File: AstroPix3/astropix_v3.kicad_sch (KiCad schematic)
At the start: 50 parts, among them J1 pcie_GECCO, J10 SPI_right, J2 ChipRings, J3 TempSens, J4 SFOut, J5 sample_clock_out, J6 HV_in_external, J7 Conn_01x03, J9 SPI_left, U2 SN65LVDS4, U5 AstroPix3_split

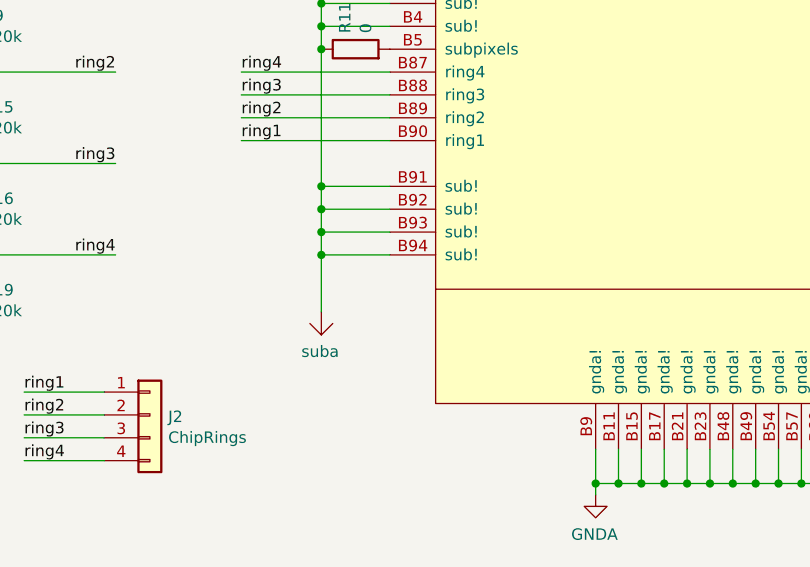
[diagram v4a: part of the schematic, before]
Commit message: PCB: Connected HV Pad
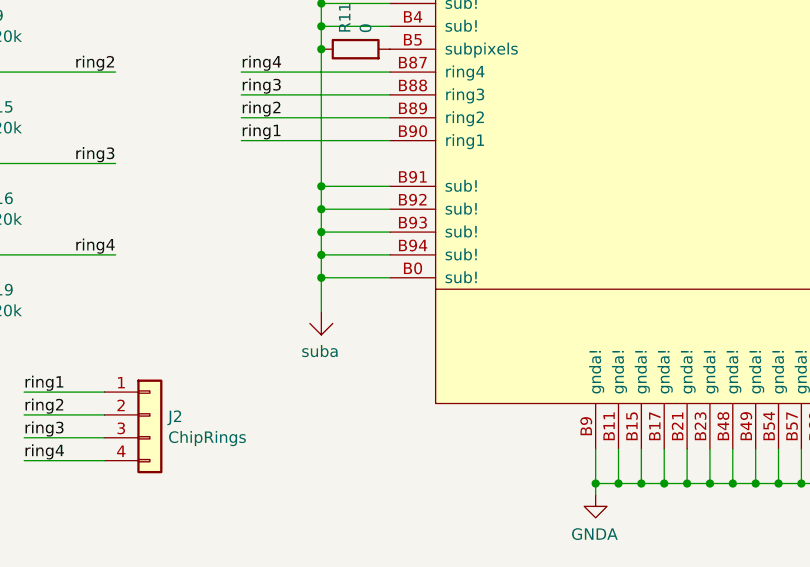
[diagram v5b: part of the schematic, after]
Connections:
- net suba: now also U5.B0 (sub!)
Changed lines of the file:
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@@
   (junction (at 309.88 236.22) (diameter 0) (color 0 0 0 0)
+  )
+  (junction (at 266.7 213.36) (diameter 0) (color 0 0 0 0)
   )
   (junction (at 266.7 203.2) (diameter 0) (color 0 0 0 0)
@@
     (stroke (width 0) (type default) (color 0 0 0 0))
   )
+  (wire (pts (xy 266.7 213.36) (xy 274.32 213.36))
+    (stroke (width 0) (type default) (color 0 0 0 0))
+  )
   (wire (pts (xy 266.7 208.28) (xy 266.7 205.74))
     (stroke (width 0) (type default) (color 0 0 0 0))
@@
     (stroke (width 0) (type default) (color 0 0 0 0))
   )
-  (wire (pts (xy 266.7 210.82) (xy 266.7 217.17))
+  (wire (pts (xy 266.7 210.82) (xy 266.7 213.36))
     (stroke (width 0) (type default) (color 0 0 0 0))
   )
@@
   )
   (wire (pts (xy 259.08 146.05) (xy 274.32 146.05))
+    (stroke (width 0) (type default) (color 0 0 0 0))
+  )
+  (wire (pts (xy 266.7 213.36) (xy 266.7 217.17))
     (stroke (width 0) (type default) (color 0 0 0 0))
   )
@@
     (pin "1")
   )
-  (symbol (lib_id "astropix:AstroPix3_split_power2") (at 304.8 144.78 0) (unit 1)
+  (symbol (lib_name "AstroPix3_split_power2_1") (lib_id "astropix:AstroPix3_split_power2") (at 304.8 144.78 0) (unit 1)
     (in_bom yes) (on_board yes) (fields_autoplaced)
     (property "Reference" "U5" (id 0) (at 370.84 126.7712 0))
@@
       (effects (font (size 1.27 1.27)) hide)
     )
+    (pin "B0")
     (pin "B1")
     (pin "B11")
@@
       (effects (font (size 1.27 1.27)) hide)
     )
+    (pin "B0")
     (pin "B1")
     (pin "B11")

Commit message: PCB: V3 improvements
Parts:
- removed R1: 0, Resistor_SMD:R_1206_3216Metric, symbol Device:R
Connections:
- net -HV: no longer names the net of J1.A1 (HV)
- net -HV: no longer J1.B1 (HV)
- no-connect marks 53 -> 55
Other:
- note removed: "GECCO HV Clearance?"
- moved on the sheet: J6
